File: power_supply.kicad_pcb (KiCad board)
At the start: 2 copper layers, 50 x 100 mm, 32 parts, among them P1 GND, P10 6.3_AC, P11 HEAT, P12 HEAT, P13 R+, P2 BIAS_AC, P3 BIAS_AC, P4 HT_AC, P5 HT_AC, P6 HT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

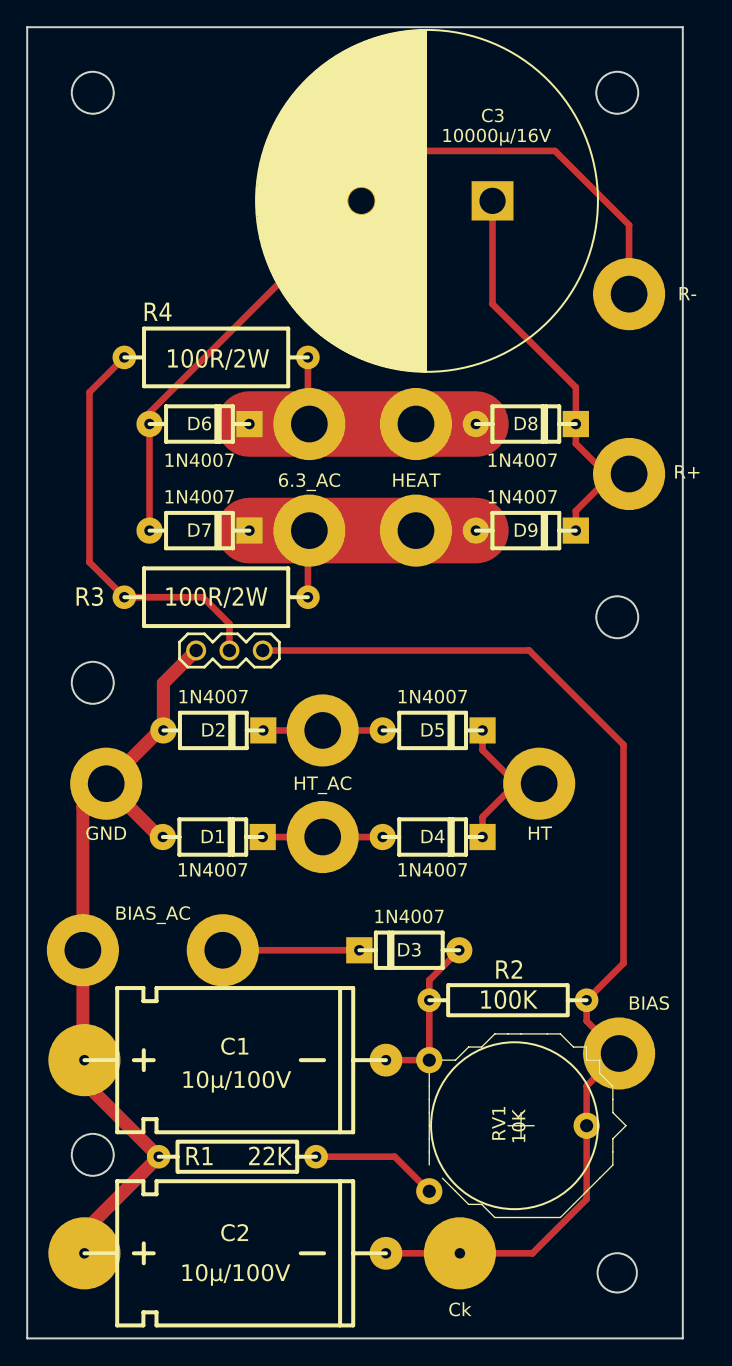
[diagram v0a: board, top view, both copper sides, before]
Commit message: Update track widths & route on both layers
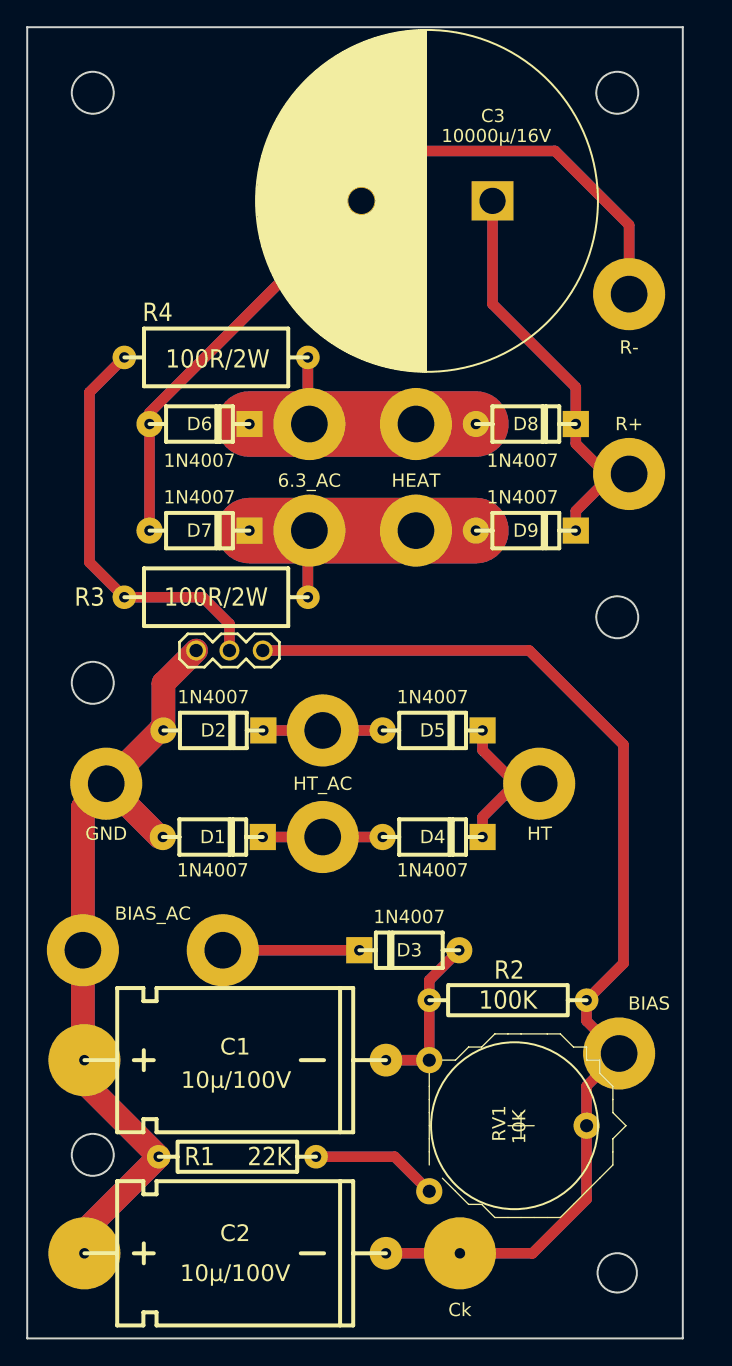
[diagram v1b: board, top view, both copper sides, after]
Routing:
- net /Vbias: track 85.4 -> 170.7 mm
- net Net-(C3-Pad2): track 61.4 -> 122.9 mm
- net GND: track 60.5 -> 120.9 mm
- net Net-(C3-Pad1): track 32.9 -> 65.8 mm
- net Net-(JP1-Pad2): track 31.4 -> 62.8 mm
- net /HEAT2: track 22.4 -> 44.8 mm
- net /HEAT1: track 22.4 -> 44.8 mm
- net Net-(C1-Pad2): track 12.6 -> 25.3 mm
- net /HT: track 13.8 -> 25.8 mm
- net Net-(D3-Pad1): track 10.4 -> 20.8 mm
- net Net-(R1-Pad2): track 9.73 -> 19.5 mm
- net /HT1: track 9.14 -> 18.3 mm
- net /HT2: track 9.10 -> 18.2 mm
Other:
- net class Default: clearance 0.5 -> 0.8; trace_width 0.5 -> 0.8
- net class GND: clearance 0.5 -> 0.8; trace_width 1 -> 1.8
- net class HEAT: clearance 0.5 -> 0.8
- net class HT: trace_width 0.5 -> 0.8
- rule trace_clearance: 0.5 -> 0.8

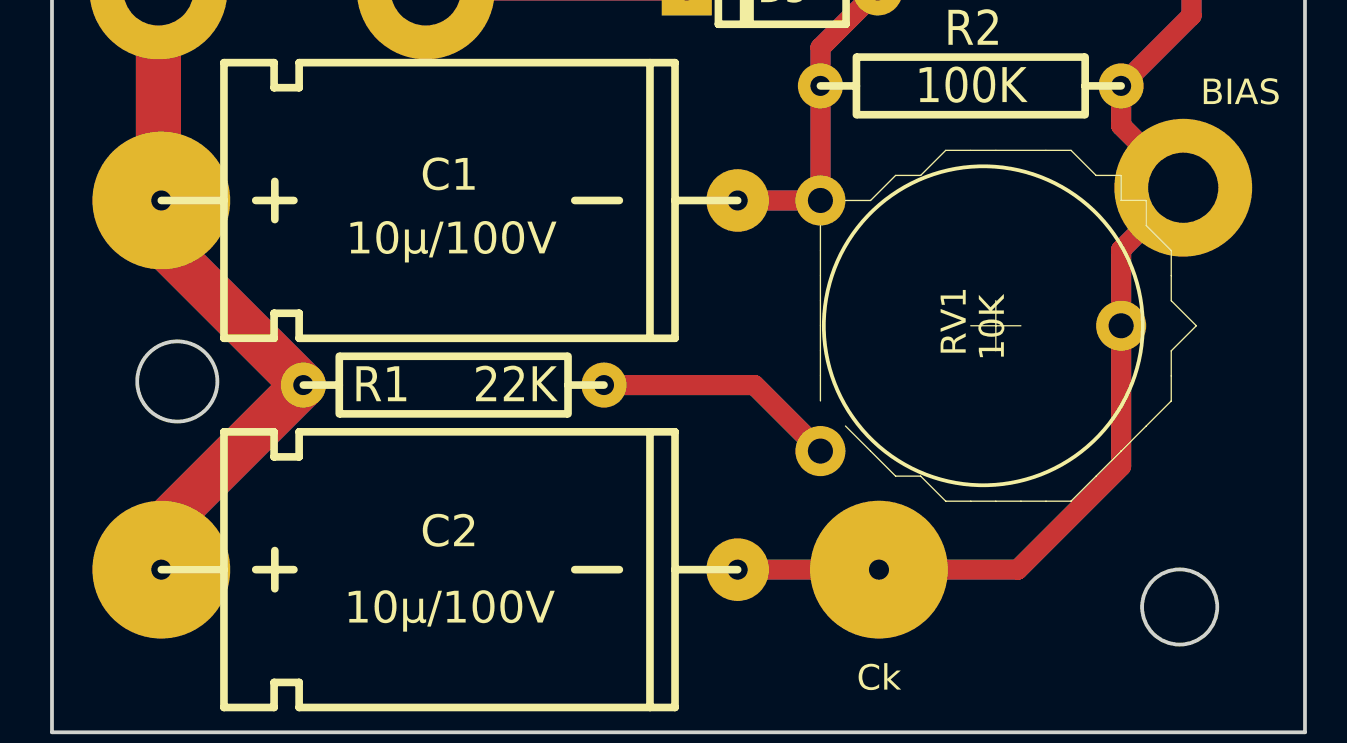
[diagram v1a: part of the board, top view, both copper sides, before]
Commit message: Fix tracks near fixation hole & pot too close to bias turret
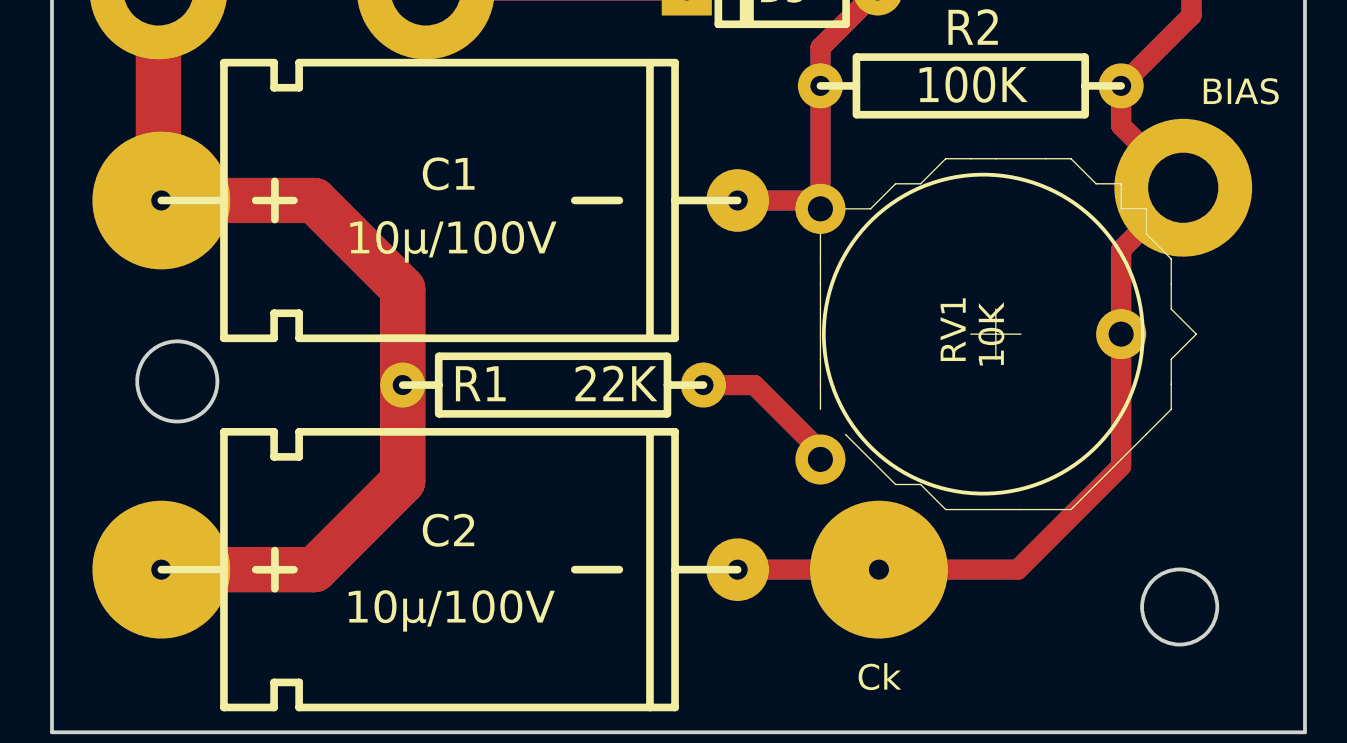
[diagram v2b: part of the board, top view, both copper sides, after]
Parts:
- moved R1 3.97 mm to (95.0, 136.1)
- moved RV1 0.33 mm to (105.7, 129.1)
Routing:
- net GND: track 120.9 -> 141.8 mm
- net Net-(R1-Pad2): track 19.5 -> 11.5 mm
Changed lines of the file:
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@@
-(kicad_pcb (version 4) (host pcbnew 4.0.2+dfsg1-stable)
+(kicad_pcb (version 4) (host pcbnew 4.0.4+dfsg1-stable)
   (general
     (links 39)
@@
     (thickness 1.6)
     (drawings 10)
-    (tracks 155)
+    (tracks 159)
     (zones 0)
     (modules 32)
@@
   )
   (module ay_passive:R_0.5W (layer F.Cu)
-    (at 91.028 136.144)
+    (at 94.996 136.144)
     (descr "Resistance 1/2W")
     (tags R)
@@
   )
   (module Potentiometers:Potentiometer_Trimmer-Piher_PT15-V12-5_horizontal (layer F.Cu)
-    (at 105.664 128.778 270)
+    (at 105.664 129.112 270)
     (descr "Potentiometer, Trimmer, Piher, PT15, Type V12.5, horizontal, Rev A, 02 Aug 2010,")
     (tags "Potentiometer, Trimmer, Piher, PT15, Type V12.5, horizontal, Rev A, 02 Aug 2010,")
@@
   (gr_line (start 125 50) (end 125 150) (layer Edge.Cuts) (width 0.15))
   (gr_line (start 75 50) (end 125 50) (layer Edge.Cuts) (width 0.15))
-  (segment (start 79.362 143.51) (end 79.362 141.81) (width 1.8) (layer B.Cu) (net 1))
-  (segment (start 79.362 141.81) (end 85.028 136.144) (width 1.8) (layer B.Cu) (net 1))
-  (segment (start 79.362 128.778) (end 79.362 130.478) (width 1.8) (layer B.Cu) (net 1))
-  (segment (start 79.362 130.478) (end 85.028 136.144) (width 1.8) (layer B.Cu) (net 1))
+  (segment (start 85.471 128.778) (end 88.996 132.303) (width 1.8) (layer B.Cu) (net 1))
+  (segment (start 88.996 132.303) (end 88.996 136.144) (width 1.8) (layer B.Cu) (net 1))
+  (segment (start 79.362 128.778) (end 85.471 128.778) (width 1.8) (layer B.Cu) (net 1))
+  (segment (start 85.471 143.51) (end 88.996 139.985) (width 1.8) (layer B.Cu) (net 1))
+  (segment (start 88.996 139.985) (end 88.996 136.144) (width 1.8) (layer B.Cu) (net 1))
+  (segment (start 79.362 143.51) (end 85.471 143.51) (width 1.8) (layer B.Cu) (net 1))
+  (segment (start 85.471 143.51) (end 88.996 139.985) (width 1.8) (layer F.Cu) (net 1))
+  (segment (start 88.996 139.985) (end 88.996 136.144) (width 1.8) (layer F.Cu) (net 1))
+  (segment (start 79.362 143.51) (end 85.471 143.51) (width 1.8) (layer F.Cu) (net 1))
+  (segment (start 85.471 128.778) (end 88.996 132.303) (width 1.8) (layer F.Cu) (net 1))
+  (segment (start 88.996 132.303) (end 88.996 136.144) (width 1.8) (layer F.Cu) (net 1))
+  (segment (start 79.362 128.778) (end 85.471 128.778) (width 1.8) (layer F.Cu) (net 1))
   (segment (start 79.248 120.396) (end 79.248 128.664) (width 1.8) (layer B.Cu) (net 1))
   (segment (start 79.248 128.664) (end 79.362 128.778) (width 1.8) (layer B.Cu) (net 1))
@@
   (segment (start 79.248 109.474) (end 81.026 107.696) (width 1.8) (layer F.Cu) (net 1))
   (segment (start 79.248 120.396) (end 79.248 109.474) (width 1.8) (layer F.Cu) (net 1))
-  (segment (start 79.362 141.81) (end 85.028 136.144) (width 1.8) (layer F.Cu) (net 1))
-  (segment (start 79.362 143.51) (end 79.362 141.81) (width 1.8) (layer F.Cu) (net 1))
-  (segment (start 79.362 128.778) (end 79.362 130.478) (width 1.8) (layer F.Cu) (net 1))
-  (segment (start 79.362 130.478) (end 85.028 136.144) (width 1.8) (layer F.Cu) (net 1))
   (segment (start 85.388 103.632) (end 85.09 103.632) (width 1) (layer F.Cu) (net 1))
   (segment (start 85.09 103.632) (end 81.026 107.696) (width 1.8) (layer F.Cu) (net 1))
@@
   (segment (start 88.392 93.472) (end 90.424 95.504) (width 0.8) (layer F.Cu) (net 7))
   (segment (start 82.408 93.472) (end 88.392 93.472) (width 0.8) (layer F.Cu) (net 7))
-  (segment (start 97.028 136.144) (end 103.03 136.144) (width 0.8) (layer B.Cu) (net 8))
+  (segment (start 100.996 136.144) (end 103.03 136.144) (width 0.8) (layer B.Cu) (net 8))
   (segment (start 103.03 136.144) (end 105.664 138.778) (width 0.8) (layer B.Cu) (net 8))
+  (segment (start 100.996 136.144) (end 103.03 136.144) (width 0.8) (layer F.Cu) (net 8))
   (segment (start 103.03 136.144) (end 105.664 138.778) (width 0.8) (layer F.Cu) (net 8))
-  (segment (start 97.028 136.144) (end 103.03 136.144) (width 0.8) (layer F.Cu) (net 8))
   (segment (start 96.408 75.184) (end 96.408 80.152) (width 0.8) (layer B.Cu) (net 9))
   (segment (start 96.408 80.152) (end 96.52 80.264) (width 0.8) (layer B.Cu) (net 9))

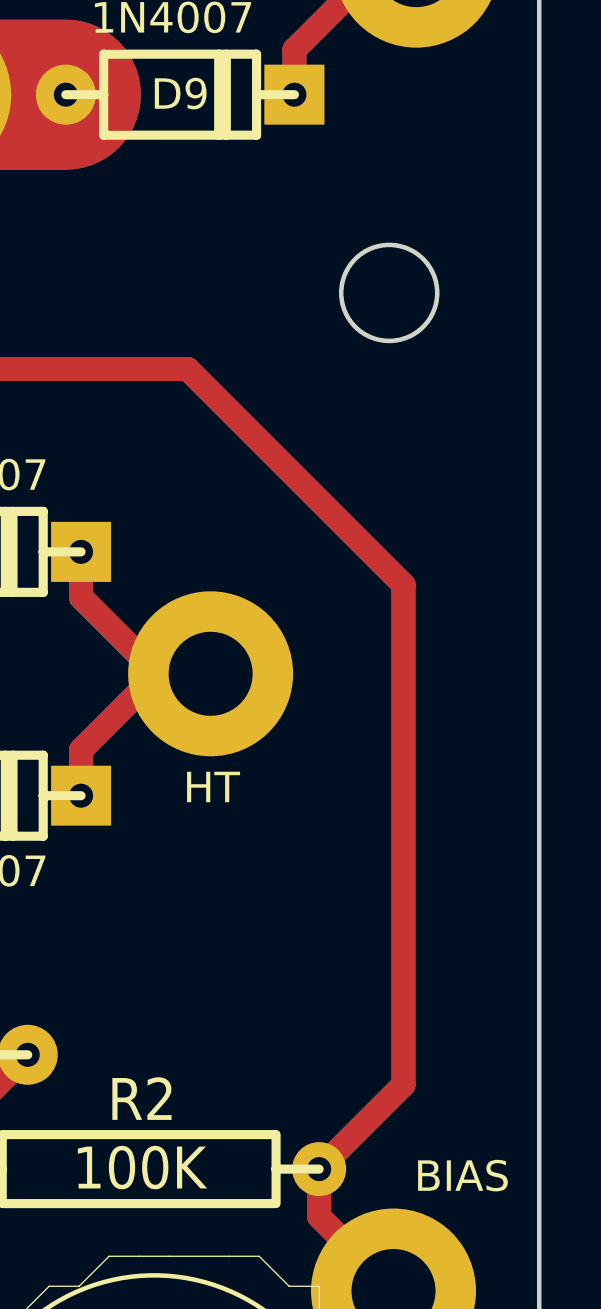
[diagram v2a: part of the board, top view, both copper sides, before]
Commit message: Regenerate drill file & add project name
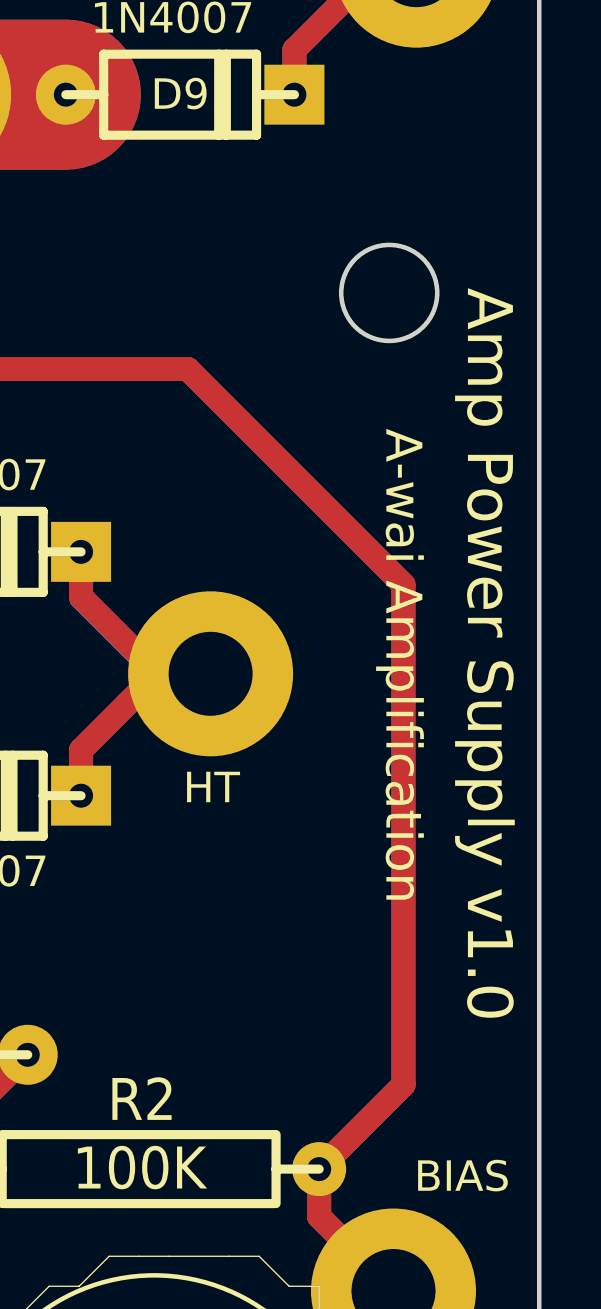
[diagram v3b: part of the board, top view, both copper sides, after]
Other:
- board text added: "A-wai Amplification"
- board text added: "Amp Power Supply v1.0"
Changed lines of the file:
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@@
     (area 70.057499 47.420999 130.094501 152.700501)
     (thickness 1.6)
-    (drawings 10)
+    (drawings 12)
     (tracks 159)
     (zones 0)
@@
       (net 3 /Vbias) (clearance 0.5))
   )
+  (gr_text "A-wai Amplification" (at 120.4595 107.442 270) (layer F.SilkS)
+    (effects (font (size 1.2 1.2) (thickness 0.25)))
+  )
+  (gr_text "Amp Power Supply v1.0" (at 123.317 107.061 270) (layer F.SilkS)
+    (effects (font (size 1.5 1.5) (thickness 0.3)))
+  )
   (gr_circle (center 80 136) (end 81.6 136) (layer Edge.Cuts) (width 0.15))
